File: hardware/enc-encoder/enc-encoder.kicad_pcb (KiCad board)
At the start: 4 copper layers, 40 x 40 mm, 84 parts, among them J1 OQ0232510000G, J2 OQ0232510000G, J3 USB_C_Receptacle, J4 SM03B-SRSS-TB, J5 OQ0232510000G, J6 OQ0232510000G, SW1 219-4LPSTR, U1 RP2350A, U2 W25Q128JVS, U3 AS5600, U4 SP3485CN, Y1 ABM8-272-T3

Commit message: added fiducials for PNP and silkscreen
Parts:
- removed ZEH: LOGO, Tags:Zeph
- added FID1: Fiducial, Fiducial:Fiducial_0.75mm_Mask1.5mm, F.Cu at (147.7, 100.2)
- added FID2: Fiducial, Fiducial:Fiducial_0.75mm_Mask1.5mm, F.Cu at (136.0, 118.8)
- added FID3: Fiducial, Fiducial:Fiducial_0.75mm_Mask1.5mm, F.Cu at (164.0, 118.6)
- added G***: LOGO, LOGO, B.Cu at (135.9, 98.1)
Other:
- board text added: "! 5-24V IN !"
- board text added: "! DIAMETRIC MAG !"
- board text added: "! RS485 !"
- board text added: "ADDRESS SPACE: 0-7 000 -> ID 0 111 -> ID 7 DEFAULT DIR: CW"
- board text added: "ORIGIN"
- board text added: "ROAR"
- board text added: "TAKE US TO THE STARS!"
- board text added: "USB PROG DVI"
- board text added: "ZH MB"
- board text removed: "Quack"
- board text removed: "ZH"

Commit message: Fix: Typo and missing model reference
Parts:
- removed the G*** at (135.9, 98.1)
- added ZEH: LOGO, LOGO, B.Cu at (166.1, 104.8)
- moved FID1 0.20 mm to (147.7, 100.0)

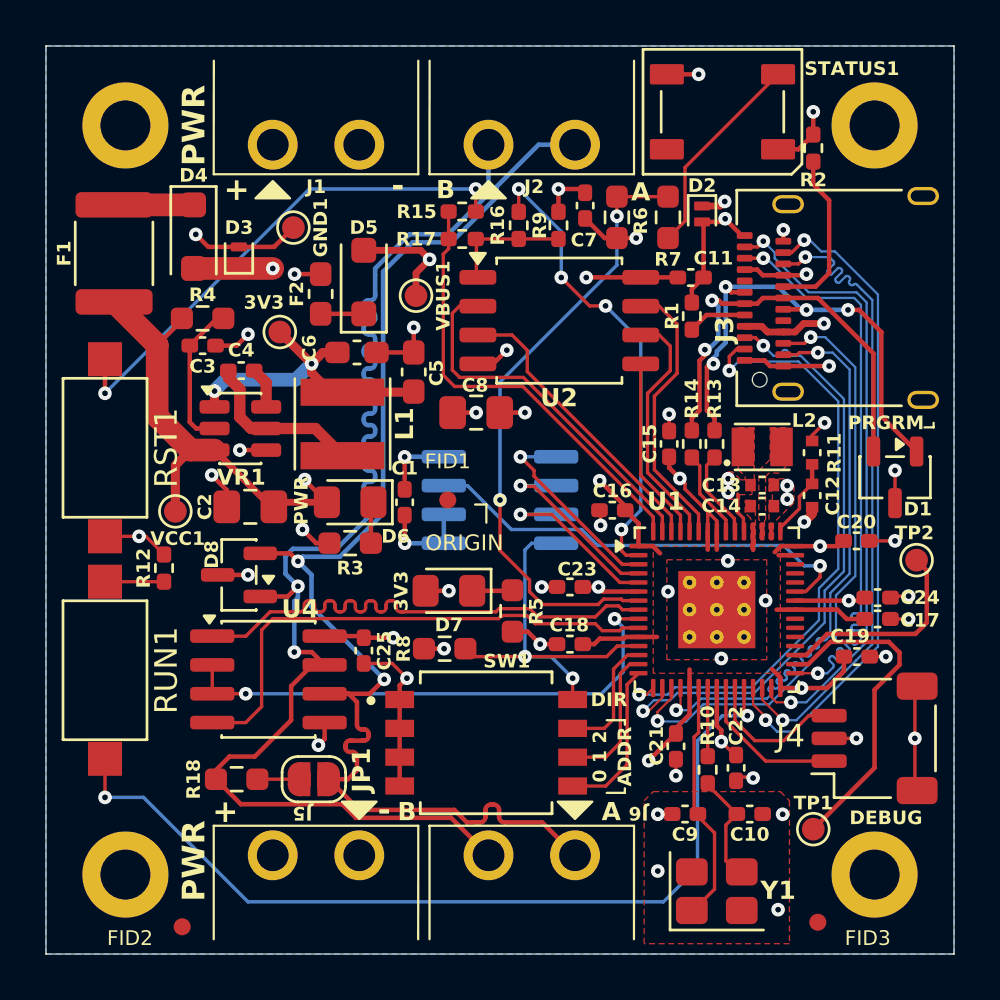
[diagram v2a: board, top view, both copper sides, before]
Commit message: fixed knockout silkscreen and added more ground return paths
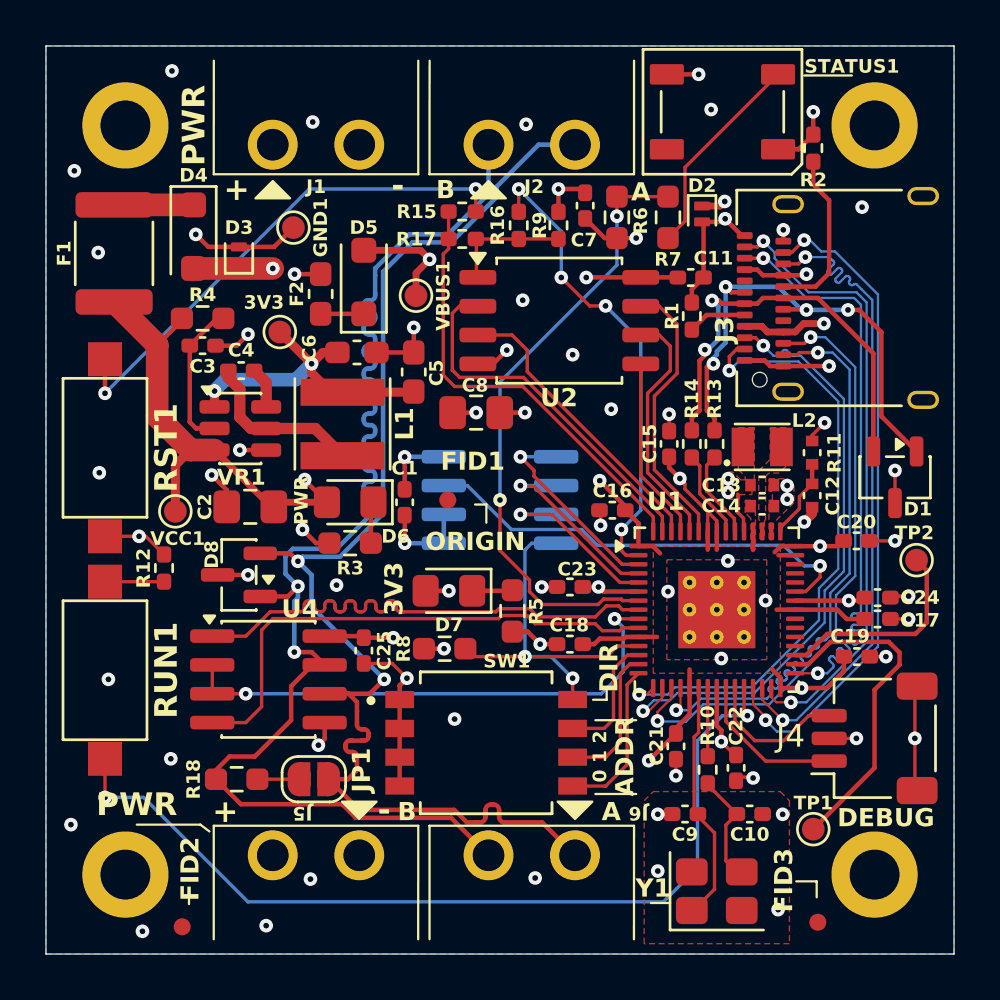
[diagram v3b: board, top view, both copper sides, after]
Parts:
- removed G***: LOGO, Tags:Goose
- moved ZEH 15.9 mm to (150.9, 109.6)
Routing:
- net GND: vias 38 -> 58
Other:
- board text removed: "HONK >"
- board text removed: "PRGRM"
